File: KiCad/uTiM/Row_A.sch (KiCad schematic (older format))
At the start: 16 parts, among them U101 APA102, U102 APA102, U103 APA102, U104 APA102, U105 APA102, U106 APA102, U107 APA102, U108 APA102

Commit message: microTiM aka uTiM work in progress
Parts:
- S101: value CONN_1 -> DI_A; footprint TinyTiM_Libs:Screw_SSide -> TinyTiM_Libs:Contact_SMD
- S102: value CONN_1 -> CI_A; footprint TinyTiM_Libs:Screw_SSide -> TinyTiM_Libs:Contact_SMD
- S103, S104, S105, S106: value CONN_1 -> MH
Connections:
- net CO_A renamed CI_B
- net DO_A renamed DI_B
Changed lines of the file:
@@
 P 4600 6650
 F 0 "S101" V 4680 6650 40  0000 L CNN
-F 1 "CONN_1" H 4600 6705 30  0001 C CNN
-F 2 "TinyTiM_Libs:Screw_SSide" H 4600 6805 30  0001 C CNN
+F 1 "DI_A" H 4600 6705 30  0001 C CNN
+F 2 "TinyTiM_Libs:Contact_SMD" H 4600 6805 30  0001 C CNN
 F 3 "" H 4600 6650 60  0001 C CNN
 	1    4600 6650
@@
 P 5150 6650
 F 0 "S102" V 5230 6650 40  0000 L CNN
-F 1 "CONN_1" H 5150 6705 30  0001 C CNN
-F 2 "TinyTiM_Libs:Screw_SSide" H 5150 6805 30  0001 C CNN
+F 1 "CI_A" H 5150 6705 30  0001 C CNN
+F 2 "TinyTiM_Libs:Contact_SMD" H 5150 6805 30  0001 C CNN
 F 3 "" H 5150 6650 60  0001 C CNN
 	1    5150 6650
@@
 P 5700 6650
 F 0 "S103" V 5780 6650 40  0000 L CNN
-F 1 "CONN_1" H 5700 6705 30  0001 C CNN
+F 1 "MH" H 5700 6705 30  0001 C CNN
 F 2 "TinyTiM_Libs:Screw_NPTH" H 5700 6805 30  0001 C CNN
 F 3 "" H 5700 6650 60  0001 C CNN
@@
 P 5900 6650
 F 0 "S104" V 5980 6650 40  0000 L CNN
-F 1 "CONN_1" H 5900 6705 30  0001 C CNN
+F 1 "MH" H 5900 6705 30  0001 C CNN
 F 2 "TinyTiM_Libs:Screw_NPTH" H 5900 6805 30  0001 C CNN
 F 3 "" H 5900 6650 60  0001 C CNN
@@
 DI_A
 Text HLabel 950  3100 0    60   Output ~ 12
-CO_A
+CI_B
 Text HLabel 950  2350 0    60   Input ~ 12
 GND
@@
 5V
 Text Label 1075 3100 0    60   ~ 0
-CO_A
+CI_B
 $Comp
 L GND #PWR011
@@
 	10950 3350 950  3350
 Text HLabel 950  3350 0    60   Output ~ 12
-DO_A
+DI_B
 Text HLabel 950  1400 0    60   Input ~ 12
 DI_A
@@
 	1300 1600 950  1600
 Text Label 1075 3350 0    60   ~ 0
-DO_A
+DI_B
 Text Label 1075 1600 0    60   ~ 0
 CI_A
@@
 P 5700 6850
 F 0 "S105" V 5780 6850 40  0000 L CNN
-F 1 "CONN_1" H 5700 6905 30  0001 C CNN
+F 1 "MH" H 5700 6905 30  0001 C CNN
 F 2 "TinyTiM_Libs:Screw_NPTH" H 5700 7005 30  0001 C CNN
 F 3 "" H 5700 6850 60  0001 C CNN
@@
 P 5900 6850
 F 0 "S106" V 5980 6850 40  0000 L CNN
-F 1 "CONN_1" H 5900 6905 30  0001 C CNN
+F 1 "MH" H 5900 6905 30  0001 C CNN
 F 2 "TinyTiM_Libs:Screw_NPTH" H 5900 7005 30  0001 C CNN
 F 3 "" H 5900 6850 60  0001 C CNN

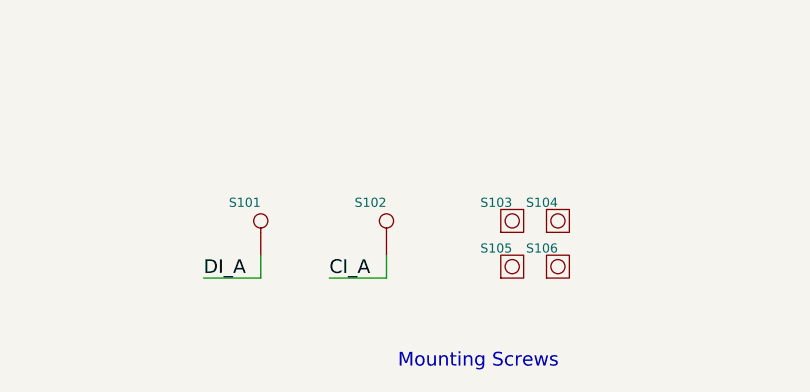
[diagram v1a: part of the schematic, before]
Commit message: work in progress, microTIM using APA102
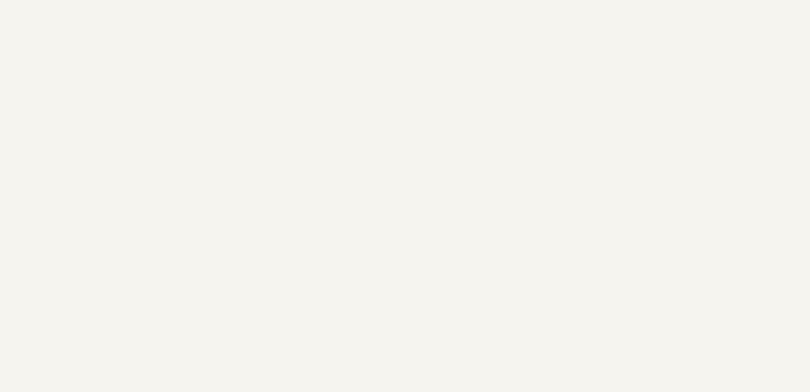
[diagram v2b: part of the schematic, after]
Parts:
- removed S101: DI_A, TinyTiM_Libs:Contact_SMD, symbol CONN_1
- removed S102: CI_A, TinyTiM_Libs:Contact_SMD, symbol CONN_1
- removed S103, S104, S105, S106: MH, TinyTiM_Libs:Screw_NPTH, symbol LOGO_1
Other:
- note removed: "Mounting Screws"
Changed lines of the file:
@@
 	1    0    0    -1
 $EndComp
-$Comp
-L CONN_1 S101
-U 1 1 5118AB77
-P 4600 6650
-F 0 "S101" V 4680 6650 40  0000 L CNN
-F 1 "DI_A" H 4600 6705 30  0001 C CNN
-F 2 "TinyTiM_Libs:Contact_SMD" H 4600 6805 30  0001 C CNN
-F 3 "" H 4600 6650 60  0001 C CNN
-	1    4600 6650
-	0    -1   -1   0
-$EndComp
-$Comp
-L CONN_1 S102
-U 1 1 5118AB75
-P 5150 6650
-F 0 "S102" V 5230 6650 40  0000 L CNN
-F 1 "CI_A" H 5150 6705 30  0001 C CNN
-F 2 "TinyTiM_Libs:Contact_SMD" H 5150 6805 30  0001 C CNN
-F 3 "" H 5150 6650 60  0001 C CNN
-	1    5150 6650
-	0    -1   -1   0
-$EndComp
-Text Notes 5200 7300 0    60   ~ 0
-Mounting Screws
 Text Label 1250 6350 0    60   ~ 0
 5V
@@
 Wire Wire Line
 	1250 6550 1250 6350
-$Comp
-L LOGO_1 S103
-U 1 1 5356BD57
-P 5700 6650
-F 0 "S103" V 5780 6650 40  0000 L CNN
-F 1 "MH" H 5700 6705 30  0001 C CNN
-F 2 "TinyTiM_Libs:Screw_NPTH" H 5700 6805 30  0001 C CNN
-F 3 "" H 5700 6650 60  0001 C CNN
-	1    5700 6650
-	0    -1   -1   0
-$EndComp
-$Comp
-L LOGO_1 S104
-U 1 1 5356BD5D
-P 5900 6650
-F 0 "S104" V 5980 6650 40  0000 L CNN
-F 1 "MH" H 5900 6705 30  0001 C CNN
-F 2 "TinyTiM_Libs:Screw_NPTH" H 5900 6805 30  0001 C CNN
-F 3 "" H 5900 6650 60  0001 C CNN
-	1    5900 6650
-	0    -1   -1   0
-$EndComp
-Wire Wire Line
-	4600 6800 4600 6900
-Wire Wire Line
-	4600 6900 4350 6900
-Wire Wire Line
-	5150 6800 5150 6900
-Wire Wire Line
-	5150 6900 4900 6900
-Text Label 4350 6900 0    60   ~ 0
-DI_A
-Text Label 4900 6900 0    60   ~ 0
-CI_A
 Text Label 1075 1400 0    60   ~ 0
 DI_A
@@
 Text Label 1075 1600 0    60   ~ 0
 CI_A
-$Comp
-L LOGO_1 S105
-U 1 1 56C43470
-P 5700 6850
-F 0 "S105" V 5780 6850 40  0000 L CNN
-F 1 "MH" H 5700 6905 30  0001 C CNN
-F 2 "TinyTiM_Libs:Screw_NPTH" H 5700 7005 30  0001 C CNN
-F 3 "" H 5700 6850 60  0001 C CNN
-	1    5700 6850
-	0    -1   -1   0
-$EndComp
-$Comp
-L LOGO_1 S106
-U 1 1 56C43845
-P 5900 6850
-F 0 "S106" V 5980 6850 40  0000 L CNN
-F 1 "MH" H 5900 6905 30  0001 C CNN
-F 2 "TinyTiM_Libs:Screw_NPTH" H 5900 7005 30  0001 C CNN
-F 3 "" H 5900 6850 60  0001 C CNN
-	1    5900 6850
-	0    -1   -1   0
-$EndComp
 $EndSCHEMATC

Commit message: layout complete. Gerbers pending
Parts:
- C2: renamed from C117; manf# (none) -> Value
- renumbered C101 to C1, U101 to U01, U102 to U02, U103 to U03, U104 to U04, U105 to U05, U106 to U06, U107 to U07, U108 to U08
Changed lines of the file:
@@
 $EndDescr
 $Comp
-L C2 C101
+L C2 C1
 U 1 1 5118AB57
 P 1800 2600
-F 0 "C101" H 1825 2700 40  0000 L CNB
+F 0 "C1" H 1825 2700 40  0000 L CNB
 F 1 "100n" H 1825 2500 40  0000 L CNN
 F 2 "TinyTiM_Libs:c_0805" H 1800 2600 50  0001 C CNN
@@
 GND
 $Comp
-L C_POL_1 C117
+L C_POL_1 C2
 U 1 1 5118AB5E
 P 1250 6750
-F 0 "C117" H 1375 6725 40  0000 L CNB
+F 0 "C2" H 1375 6725 40  0000 L CNB
 F 1 "47u,8V" H 1375 6625 40  0000 L CNN
 F 2 "TinyTiM_Libs:c_2917" H 1250 6700 50  0001 C CNN
 F 3 "" H 1250 6750 60  0001 C CNN
-F 4 "CAP ALUM 47UF 8V 20% SMD" H 1250 6950 60  0001 L CNN "Field4"
-F 5 "47u,8V" H 1250 7050 60  0001 L CNN "Field5"
-F 6 "2917 (7343 Metric)" H 1250 7150 60  0001 L CNN "Field6"
-F 7 "Panasonic Electronic Components" H 1250 7250 60  0001 L CNN "Field7"
-F 8 "EEF-CD0K470R" H 1250 7350 60  0001 L CNN "Field8"
-F 9 "Digikey" H 1250 7450 60  0001 L CNN "Field9"
-F 10 "PCE3606CT-ND" H 1250 7550 60  0001 L CNN "Field10"
-F 11 "http://www.digikey.com/product-detail/en/EEF-CD0K470R/PCE3606CT-ND/614442" H 1250 7650 60  0001 L CNN "Field11"
+F 4 "Value" H 1250 6750 60  0001 C CNN "manf#"
+F 5 "CAP ALUM 47UF 8V 20% SMD" H 1250 6950 60  0001 L CNN "Field4"
+F 6 "47u,8V" H 1250 7050 60  0001 L CNN "Field5"
+F 7 "2917 (7343 Metric)" H 1250 7150 60  0001 L CNN "Field6"
+F 8 "Panasonic Electronic Components" H 1250 7250 60  0001 L CNN "Field7"
+F 9 "EEF-CD0K470R" H 1250 7350 60  0001 L CNN "Field8"
+F 10 "Digikey" H 1250 7450 60  0001 L CNN "Field9"
+F 11 "PCE3606CT-ND" H 1250 7550 60  0001 L CNN "Field10"
+F 12 "http://www.digikey.com/product-detail/en/EEF-CD0K470R/PCE3606CT-ND/614442" H 1250 7650 60  0001 L CNN "Field11"
 	1    1250 6750
 	1    0    0    -1
@@
 GND
 $Comp
-L APA102 U101
+L APA102 U01
 U 1 1 56C2E1C1
 P 1700 1600
-F 0 "U101" H 1700 1900 40  0000 C CNB
+F 0 "U01" H 1700 1900 40  0000 C CNB
 F 1 "APA102" H 1700 1275 40  0000 C CNN
 F 2 "TinyTiM_Libs:APA102" H 1600 2000 60  0001 C CNN
@@
 5V
 $Comp
-L APA102 U102
+L APA102 U02
 U 1 1 56C2E1EC
 P 2900 1600
-F 0 "U102" H 2900 1900 40  0000 C CNB
+F 0 "U02" H 2900 1900 40  0000 C CNB
 F 1 "APA102" H 2900 1275 40  0000 C CNN
 F 2 "TinyTiM_Libs:APA102" H 2800 2000 60  0001 C CNN
@@
 $EndComp
 $Comp
-L APA102 U103
+L APA102 U03
 U 1 1 56C2E1F4
 P 4100 1600
-F 0 "U103" H 4100 1900 40  0000 C CNB
+F 0 "U03" H 4100 1900 40  0000 C CNB
 F 1 "APA102" H 4100 1275 40  0000 C CNN
 F 2 "TinyTiM_Libs:APA102" H 4000 2000 60  0001 C CNN
@@
 $EndComp
 $Comp
-L APA102 U104
+L APA102 U04
 U 1 1 56C2E1FC
 P 5300 1600
-F 0 "U104" H 5300 1900 40  0000 C CNB
+F 0 "U04" H 5300 1900 40  0000 C CNB
 F 1 "APA102" H 5300 1275 40  0000 C CNN
 F 2 "TinyTiM_Libs:APA102" H 5200 2000 60  0001 C CNN
@@
 $EndComp
 $Comp
-L APA102 U105
+L APA102 U05
 U 1 1 56C2E204
 P 6500 1600
-F 0 "U105" H 6500 1900 40  0000 C CNB
+F 0 "U05" H 6500 1900 40  0000 C CNB
 F 1 "APA102" H 6500 1275 40  0000 C CNN
 F 2 "TinyTiM_Libs:APA102" H 6400 2000 60  0001 C CNN
@@
 $EndComp
 $Comp
-L APA102 U106
+L APA102 U06
 U 1 1 56C2E20C
 P 7700 1600
-F 0 "U106" H 7700 1900 40  0000 C CNB
+F 0 "U06" H 7700 1900 40  0000 C CNB
 F 1 "APA102" H 7700 1275 40  0000 C CNN
 F 2 "TinyTiM_Libs:APA102" H 7600 2000 60  0001 C CNN
@@
 $EndComp
 $Comp
-L APA102 U107
+L APA102 U07
 U 1 1 56C2E214
 P 8900 1600
-F 0 "U107" H 8900 1900 40  0000 C CNB
+F 0 "U07" H 8900 1900 40  0000 C CNB
 F 1 "APA102" H 8900 1275 40  0000 C CNN
 F 2 "TinyTiM_Libs:APA102" H 8800 2000 60  0001 C CNN
@@
 $EndComp
 $Comp
-L APA102 U108
+L APA102 U08
 U 1 1 56C2E21C
 P 10100 1600
-F 0 "U108" H 10100 1900 40  0000 C CNB
+F 0 "U08" H 10100 1900 40  0000 C CNB
 F 1 "APA102" H 10100 1275 40  0000 C CNN
 F 2 "TinyTiM_Libs:APA102" H 10000 2000 60  0001 C CNN
